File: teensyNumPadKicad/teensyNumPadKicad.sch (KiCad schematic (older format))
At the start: 59 parts, among them J1 KCDX-5S-S2, U1 Teensy++2.0_(C)

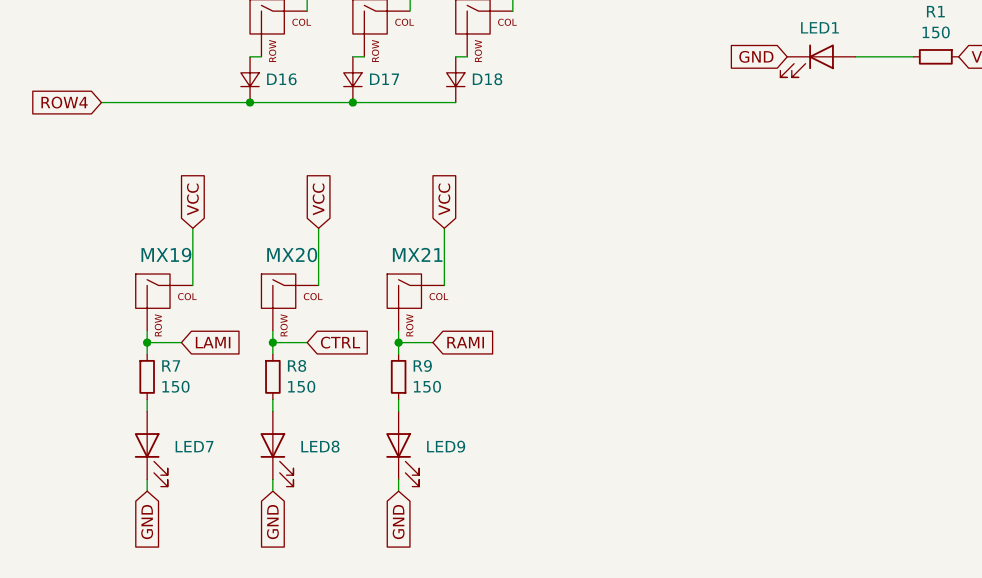
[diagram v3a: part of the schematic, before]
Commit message: Update to use MX-LED footprints where required
Use MX-LED footprints for MX-19, MX20 + MX21.
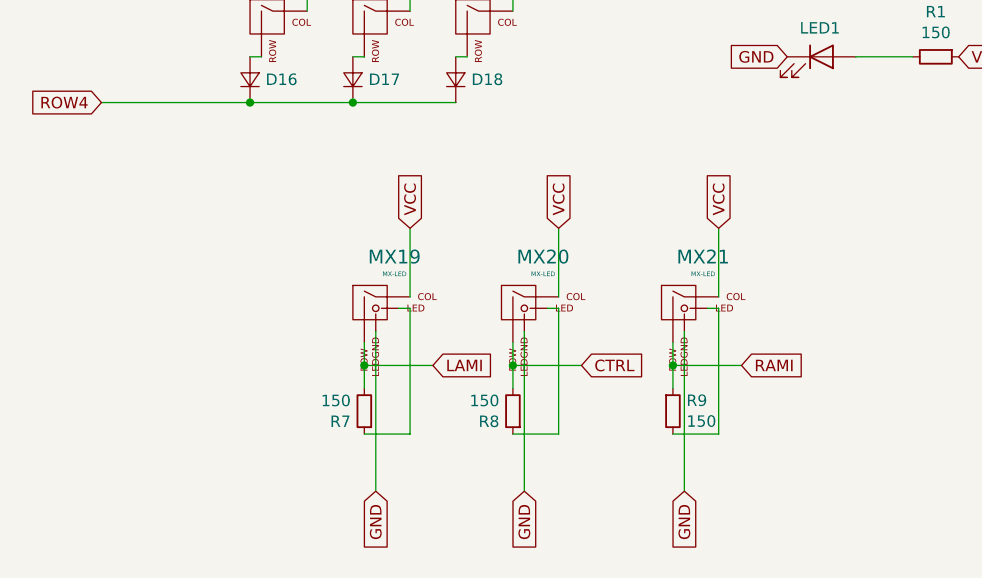
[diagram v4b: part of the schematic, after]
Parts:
- removed LED7, LED8, LED9: LED, LED_THT:LED_D3.0mm, symbol Device:LED
- removed MX19, MX20, MX21: MX-NoLED, MX_Alps_Hybrid:MX-1.25U-NoLED, symbol MX_Alps_Hybrid:MX-NoLED
- added MX19, MX20, MX21: MX-LED, MX_Alps_Hybrid:MX-1.25U, symbol MX_Alps_Hybrid:MX-LED
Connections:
- net CTRL: now also R8.2, MX20.2 (ROW); no longer R8.1
- net GND: now also MX19.4 (LEDGND), MX20.4 (LEDGND), MX21.4 (LEDGND)
- net LAMI: now also R7.2, MX19.2 (ROW); no longer R7.1
- net RAMI: now also R9.1, MX21.2 (ROW); no longer R9.2
- net VCC: now also MX19.1 (COL), MX20.1 (COL), MX21.1 (COL)
- new net: MX19.3 (LED), R7.1
- new net: MX20.3 (LED), R8.1
- new net: MX21.3 (LED), R9.2
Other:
- moved on the sheet: R7
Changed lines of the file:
@@
 Text GLabel 7250 5300 0    50   Input ~ 0
 STA3
-$Comp
-L MX_Alps_Hybrid:MX-NoLED MX19
-U 1 1 609D6C7A
-P 2100 5800
-F 0 "MX19" H 2133 5981 60  0000 C CNN
-F 1 "MX-NoLED" H 2133 5949 20  0001 C CNN
-F 2 "MX_Alps_Hybrid:MX-1.25U-NoLED" H 1475 5775 60  0001 C CNN
-F 3 "" H 1475 5775 60  0001 C CNN
-	1    2100 5800
-	1    0    0    -1
-$EndComp
-Wire Wire Line
-	2050 5950 2050 6000
-Wire Wire Line
-	2050 6000 2200 6000
-Wire Wire Line
-	2050 6000 2050 6050
-Connection ~ 2050 6000
-$Comp
-L Device:R_Small R7
-U 1 1 609DD78A
-P 2050 6150
-F 0 "R7" H 2109 6196 50  0000 L CNN
-F 1 "150" H 2109 6105 50  0000 L CNN
-F 2 "Resistor_THT:R_Axial_DIN0207_L6.3mm_D2.5mm_P10.16mm_Horizontal" H 2050 6150 50  0001 C CNN
-F 3 "~" H 2050 6150 50  0001 C CNN
-	1    2050 6150
-	1    0    0    -1
-$EndComp
-$Comp
-L Device:LED LED7
-U 1 1 609DE06B
-P 2050 6450
-F 0 "LED7" V 2043 6332 50  0000 R CNN
-F 1 "LED" V 1998 6333 50  0001 R CNN
-F 2 "LED_THT:LED_D3.0mm" H 2050 6450 50  0001 C CNN
-F 3 "~" H 2050 6450 50  0001 C CNN
-	1    2050 6450
-	0    -1   -1   0
-$EndComp
-Text GLabel 2050 6650 3    50   Input ~ 0
-GND
-Wire Wire Line
-	2050 6250 2050 6300
-Wire Wire Line
-	2050 6600 2050 6650
-Wire Wire Line
-	2250 5750 2250 5500
-Text GLabel 2250 5500 1    50   Input ~ 0
-VCC
 Text GLabel 9350 4000 2    50   Input ~ 0
 LAMI
-Text GLabel 2200 6000 2    50   Input ~ 0
-LAMI
-$Comp
-L MX_Alps_Hybrid:MX-NoLED MX20
-U 1 1 609EFA67
-P 2650 5800
-F 0 "MX20" H 2683 5981 60  0000 C CNN
-F 1 "MX-NoLED" H 2683 5949 20  0001 C CNN
-F 2 "MX_Alps_Hybrid:MX-1.25U-NoLED" H 2025 5775 60  0001 C CNN
-F 3 "" H 2025 5775 60  0001 C CNN
-	1    2650 5800
-	1    0    0    -1
-$EndComp
-Wire Wire Line
-	2600 5950 2600 6000
-Wire Wire Line
-	2600 6000 2750 6000
-Wire Wire Line
-	2600 6000 2600 6050
-Connection ~ 2600 6000
-$Comp
-L Device:R_Small R8
-U 1 1 609EFA71
-P 2600 6150
-F 0 "R8" H 2659 6196 50  0000 L CNN
-F 1 "150" H 2659 6105 50  0000 L CNN
-F 2 "Resistor_THT:R_Axial_DIN0207_L6.3mm_D2.5mm_P10.16mm_Horizontal" H 2600 6150 50  0001 C CNN
-F 3 "~" H 2600 6150 50  0001 C CNN
-	1    2600 6150
-	1    0    0    -1
-$EndComp
-$Comp
-L Device:LED LED8
-U 1 1 609EFA77
-P 2600 6450
-F 0 "LED8" V 2593 6332 50  0000 R CNN
-F 1 "LED" V 2548 6333 50  0001 R CNN
-F 2 "LED_THT:LED_D3.0mm" H 2600 6450 50  0001 C CNN
-F 3 "~" H 2600 6450 50  0001 C CNN
-	1    2600 6450
-	0    -1   -1   0
-$EndComp
-Text GLabel 2600 6650 3    50   Input ~ 0
-GND
-Wire Wire Line
-	2600 6250 2600 6300
-Wire Wire Line
-	2600 6600 2600 6650
-Wire Wire Line
-	2800 5750 2800 5500
-Text GLabel 2800 5500 1    50   Input ~ 0
-VCC
-Text GLabel 2750 6000 2    50   Input ~ 0
-CTRL
 Text GLabel 9350 4300 2    50   Input ~ 0
 CTRL
-$Comp
-L MX_Alps_Hybrid:MX-NoLED MX21
-U 1 1 609F553F
-P 3200 5800
-F 0 "MX21" H 3233 5981 60  0000 C CNN
-F 1 "MX-NoLED" H 3233 5949 20  0001 C CNN
-F 2 "MX_Alps_Hybrid:MX-1.25U-NoLED" H 2575 5775 60  0001 C CNN
-F 3 "" H 2575 5775 60  0001 C CNN
-	1    3200 5800
-	1    0    0    -1
-$EndComp
-Wire Wire Line
-	3150 5950 3150 6000
-Wire Wire Line
-	3150 6000 3300 6000
-Wire Wire Line
-	3150 6000 3150 6050
-Connection ~ 3150 6000
-$Comp
-L Device:R_Small R9
-U 1 1 609F5549
-P 3150 6150
-F 0 "R9" H 3091 6104 50  0000 R CNN
-F 1 "150" H 3091 6195 50  0000 R CNN
-F 2 "Resistor_THT:R_Axial_DIN0207_L6.3mm_D2.5mm_P10.16mm_Horizontal" H 3150 6150 50  0001 C CNN
-F 3 "~" H 3150 6150 50  0001 C CNN
-	1    3150 6150
-	-1   0    0    1
-$EndComp
-$Comp
-L Device:LED LED9
-U 1 1 609F554F
-P 3150 6450
-F 0 "LED9" V 3143 6332 50  0000 R CNN
-F 1 "LED" V 3098 6333 50  0001 R CNN
-F 2 "LED_THT:LED_D3.0mm" H 3150 6450 50  0001 C CNN
-F 3 "~" H 3150 6450 50  0001 C CNN
-	1    3150 6450
-	0    -1   -1   0
-$EndComp
-Text GLabel 3150 6650 3    50   Input ~ 0
-GND
-Wire Wire Line
-	3150 6250 3150 6300
-Wire Wire Line
-	3150 6600 3150 6650
-Wire Wire Line
-	3350 5750 3350 5500
-Text GLabel 3350 5500 1    50   Input ~ 0
-VCC
-Text GLabel 3300 6000 2    50   Input ~ 0
+Text GLabel 4650 6100 2    50   Input ~ 0
 RAMI
 Text GLabel 9350 4400 2    50   Input ~ 0
 RAMI
 NoConn ~ 4850 1800
+Wire Wire Line
+	3050 5950 3050 6650
+Wire Wire Line
+	3000 6400 3200 6400
+Wire Wire Line
+	3200 6400 3200 5850
+Wire Wire Line
+	3000 6100 3300 6100
+Connection ~ 3000 6100
+Wire Wire Line
+	3000 6100 3000 6200
+Wire Wire Line
+	3000 6100 3000 6000
+Wire Wire Line
+	3200 5850 3150 5850
+Wire Wire Line
+	3200 5800 3200 5500
+$Comp
+L MX_Alps_Hybrid:MX-LED MX19
+U 1 1 60B8188E
+P 3050 5850
+F 0 "MX19" H 3132 6074 60  0000 C CNN
+F 1 "MX-LED" H 3132 6000 20  0000 C CNN
+F 2 "MX_Alps_Hybrid:MX-1.25U" H 2425 5825 60  0001 C CNN
+F 3 "" H 2425 5825 60  0001 C CNN
+	1    3050 5850
+	1    0    0    -1
+$EndComp
+Text GLabel 3300 6100 2    50   Input ~ 0
+LAMI
+Text GLabel 3200 5500 1    50   Input ~ 0
+VCC
+Text GLabel 3050 6650 3    50   Input ~ 0
+GND
+$Comp
+L Device:R_Small R7
+U 1 1 609DD78A
+P 3000 6300
+F 0 "R7" H 3059 6346 50  0000 L CNN
+F 1 "150" H 3059 6255 50  0000 L CNN
+F 2 "Resistor_THT:R_Axial_DIN0207_L6.3mm_D2.5mm_P10.16mm_Horizontal" H 3000 6300 50  0001 C CNN
+F 3 "~" H 3000 6300 50  0001 C CNN
+	1    3000 6300
+	-1   0    0    1
+$EndComp
+Text GLabel 3950 6100 2    50   Input ~ 0
+CTRL
+Wire Wire Line
+	3700 5950 3700 6650
+Wire Wire Line
+	3650 6400 3850 6400
+Wire Wire Line
+	3850 6400 3850 5850
+Wire Wire Line
+	3650 6100 3950 6100
+Connection ~ 3650 6100
+Wire Wire Line
+	3650 6100 3650 6200
+Wire Wire Line
+	3650 6100 3650 6000
+Wire Wire Line
+	3850 5850 3800 5850
+Wire Wire Line
+	3850 5800 3850 5500
+$Comp
+L MX_Alps_Hybrid:MX-LED MX20
+U 1 1 60BC4B03
+P 3700 5850
+F 0 "MX20" H 3782 6074 60  0000 C CNN
+F 1 "MX-LED" H 3782 6000 20  0000 C CNN
+F 2 "MX_Alps_Hybrid:MX-1.25U" H 3075 5825 60  0001 C CNN
+F 3 "" H 3075 5825 60  0001 C CNN
+	1    3700 5850
+	1    0    0    -1
+$EndComp
+Text GLabel 3850 5500 1    50   Input ~ 0
+VCC
+Text GLabel 3700 6650 3    50   Input ~ 0
+GND
+$Comp
+L Device:R_Small R8
+U 1 1 60BC4B0C
+P 3650 6300
+F 0 "R8" H 3709 6346 50  0000 L CNN
+F 1 "150" H 3709 6255 50  0000 L CNN
+F 2 "Resistor_THT:R_Axial_DIN0207_L6.3mm_D2.5mm_P10.16mm_Horizontal" H 3650 6300 50  0001 C CNN
+F 3 "~" H 3650 6300 50  0001 C CNN
+	1    3650 6300
+	-1   0    0    1
+$EndComp
+Wire Wire Line
+	4400 5950 4400 6650
+Wire Wire Line
+	4350 6400 4550 6400
+Wire Wire Line
+	4550 6400 4550 5850
+Wire Wire Line
+	4350 6100 4650 6100
+Connection ~ 4350 6100
+Wire Wire Line
+	4350 6100 4350 6200
+Wire Wire Line
+	4350 6100 4350 6000
+Wire Wire Line
+	4550 5850 4500 5850
+Wire Wire Line
+	4550 5800 4550 5500
+$Comp
+L MX_Alps_Hybrid:MX-LED MX21
+U 1 1 60BD4812
+P 4400 5850
+F 0 "MX21" H 4482 6074 60  0000 C CNN
+F 1 "MX-LED" H 4482 6000 20  0000 C CNN
+F 2 "MX_Alps_Hybrid:MX-1.25U" H 3775 5825 60  0001 C CNN
+F 3 "" H 3775 5825 60  0001 C CNN
+	1    4400 5850
+	1    0    0    -1
+$EndComp
+Text GLabel 4550 5500 1    50   Input ~ 0
+VCC
+Text GLabel 4400 6650 3    50   Input ~ 0
+GND
+$Comp
+L Device:R_Small R9
+U 1 1 60BD481A
+P 4350 6300
+F 0 "R9" H 4409 6346 50  0000 L CNN
+F 1 "150" H 4409 6255 50  0000 L CNN
+F 2 "Resistor_THT:R_Axial_DIN0207_L6.3mm_D2.5mm_P10.16mm_Horizontal" H 4350 6300 50  0001 C CNN
+F 3 "~" H 4350 6300 50  0001 C CNN
+	1    4350 6300
+	1    0    0    -1
+$EndComp
 $EndSCHEMATC
